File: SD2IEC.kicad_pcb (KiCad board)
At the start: 2 copper layers, 83.8 x 53.3 mm, 22 parts, among them J1 AVR-ISP-6, J2 Cassette Port, J3 SD_Card, J4 IEC Male, J5 IEC Female, U1 ATmega644P-20AU, U2 MIC5504-3.3YM5, Y1 8MHz

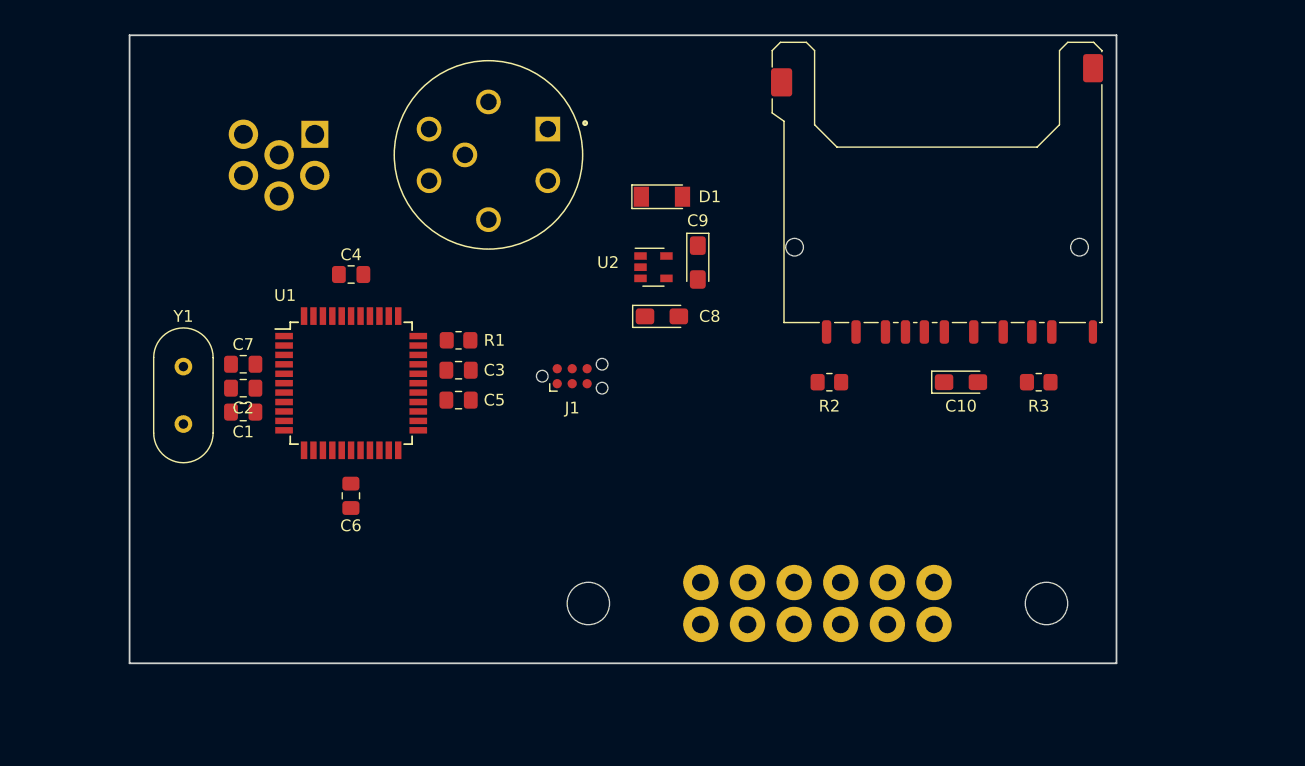
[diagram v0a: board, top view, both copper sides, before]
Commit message: Added IEC pin control
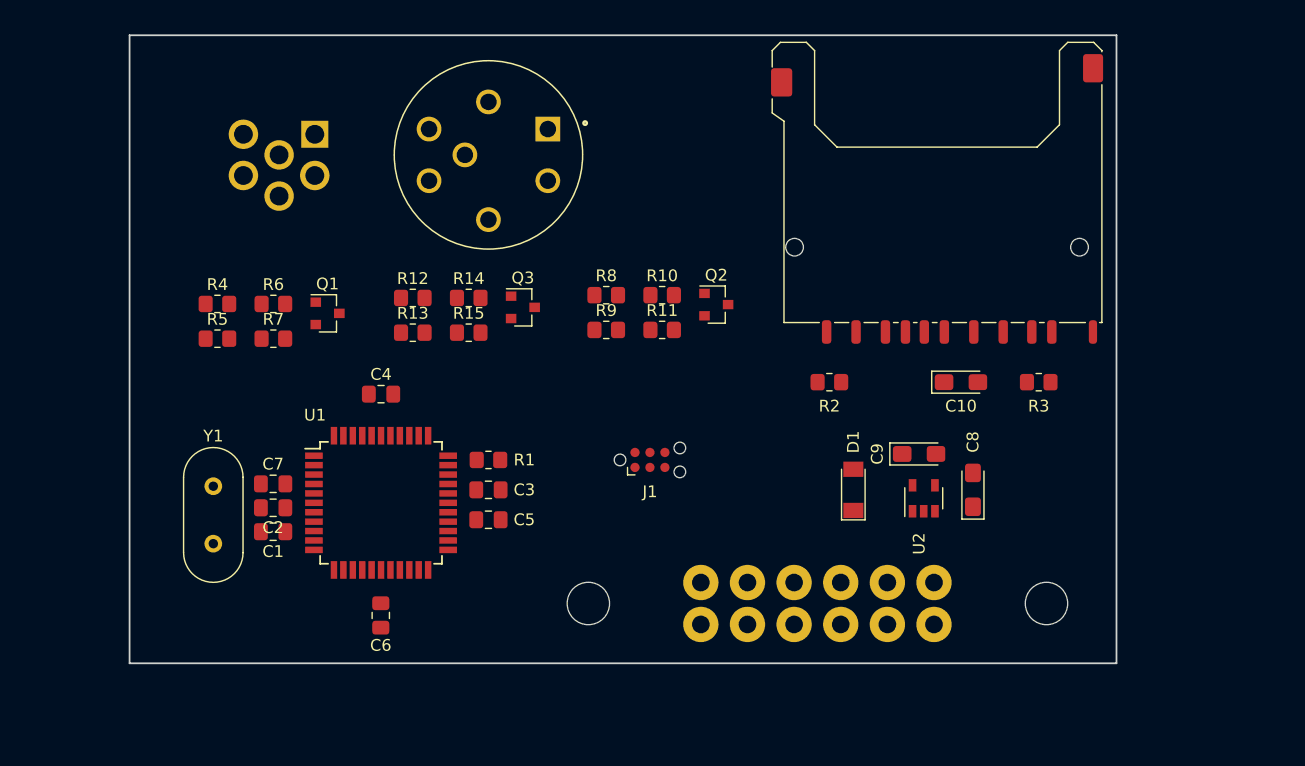
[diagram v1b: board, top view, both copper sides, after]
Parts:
- added Q1: BSS123, Package_TO_SOT_SMD:SOT-23, F.Cu at (100.6, 97.3)
- added Q2: BSS123, Package_TO_SOT_SMD:SOT-23, F.Cu at (133.7, 96.5)
- added Q3: BSS123, Package_TO_SOT_SMD:SOT-23, F.Cu at (117.2, 96.8)
- added R10: 10K, Resistor_SMD:R_0805_2012Metric_Pad1.20x1.40mm_HandSolder, F.Cu at (129.1, 95.7)
- added R11: 22K, Resistor_SMD:R_0805_2012Metric_Pad1.20x1.40mm_HandSolder, F.Cu at (129.1, 98.7)
- added R12: 10K, Resistor_SMD:R_0805_2012Metric_Pad1.20x1.40mm_HandSolder, F.Cu at (107.9, 96.0)
- added R13: 18R, Resistor_SMD:R_0805_2012Metric_Pad1.20x1.40mm_HandSolder, F.Cu at (107.9, 98.9)
- added R14: 10K, Resistor_SMD:R_0805_2012Metric_Pad1.20x1.40mm_HandSolder, F.Cu at (112.6, 96.0)
- added R15: 22K, Resistor_SMD:R_0805_2012Metric_Pad1.20x1.40mm_HandSolder, F.Cu at (112.6, 98.9)
- added R4: 10K, Resistor_SMD:R_0805_2012Metric_Pad1.20x1.40mm_HandSolder, F.Cu at (91.3, 96.5)
- added R5: 18R, Resistor_SMD:R_0805_2012Metric_Pad1.20x1.40mm_HandSolder, F.Cu at (91.3, 99.4)
- added R6: 10K, Resistor_SMD:R_0805_2012Metric_Pad1.20x1.40mm_HandSolder, F.Cu at (96.0, 96.5)
- added R7: 22K, Resistor_SMD:R_0805_2012Metric_Pad1.20x1.40mm_HandSolder, F.Cu at (96.0, 99.4)
- added R8: 10K, Resistor_SMD:R_0805_2012Metric_Pad1.20x1.40mm_HandSolder, F.Cu at (124.3, 95.7)
- added R9: 18R, Resistor_SMD:R_0805_2012Metric_Pad1.20x1.40mm_HandSolder, F.Cu at (124.3, 98.7)
- moved C8 30.2 mm to (155.4, 112.3), turned to 90 degrees
- moved U2 30.2 mm to (151.3, 113.0), turned to 90 degrees
- moved D1 29.7 mm to (145.3, 112.3), turned to 90 degrees
- moved C9 24.9 mm to (150.9, 109.2), turned to 0 degrees
- moved C6 10.5 mm to (105.2, 122.9)
- moved C7 10.5 mm to (96.0, 111.8)
- moved C5 10.5 mm to (114.3, 114.8)
- moved U1 10.5 mm to (105.2, 113.4)
- moved C1 10.5 mm to (96.0, 115.8)
- moved C2 10.5 mm to (96.0, 113.8)
- moved Y1 10.5 mm to (90.9, 116.8)
- moved C3 10.5 mm to (114.3, 112.3)
- moved C4 10.5 mm to (105.2, 104.1)
- moved R1 10.5 mm to (114.3, 109.7)
- moved J1 9.71 mm to (128.0, 109.7)
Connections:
- net IEC_ATN renamed /IEC_ATN
- net IEC_CLK renamed /IEC_CLK
- net IEC_DATA renamed /IEC_DATA
- net MISO renamed /MISO
- net MOSI renamed /MOSI
- net SCK renamed /SCK
- net ~IEC_RESET renamed /~IEC_RESET
- net ~IEC_SRQ renamed /~IEC_SQR
- net ~RESET renamed Net-(J1-Pad5)
- U1 pad 31: Net-(U1-Pad31) -> /IEC_CLK/WRITE
- U1 pad 32: Net-(U1-Pad32) -> /IEC_DATA/WRITE
- U1 pad 33: Net-(U1-Pad33) -> /IEC_ATN/WRITE
- U1 pad 35: Net-(U1-Pad35) -> /IEC_CLK/READ
- U1 pad 36: Net-(U1-Pad36) -> /IEC_DATA/READ
- U1 pad 37: Net-(U1-Pad37) -> /IEC_ATN/READ

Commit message: mosfets, switches
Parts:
- added J6: SERIAL, Connector_PinHeader_2.54mm:PinHeader_1x03_P2.54mm_Vertical, F.Cu at (91.4, 122.9)
- added SW1: IEC_SEL, Button_Switch_SMD:SW_DIP_SPSTx04_Slide_6.7x11.72mm_W8.61mm_P2.54mm_LowProfile, F.Cu at (127.0, 88.9)
- added SW2: Back, Button_Switch_THT:SW_Tactile_SPST_Angled_PTS645Vx58-2LFS, F.Cu at (118.9, 76.7)
- added SW3: Forward / Disc Change, Button_Switch_THT:SW_Tactile_SPST_Angled_PTS645Vx58-2LFS, F.Cu at (129.5, 76.7)
- Q1, Q2, Q3: value BSS123 -> AO3400A
- moved R10 21.4 mm to (107.7, 94.2)
- moved R11 21.4 mm to (107.7, 97.2)
- moved R8 21.4 mm to (103.0, 94.2)
- moved R9 21.4 mm to (103.0, 97.2)
- moved Q2 20.9 mm to (112.8, 95.5)
- moved Q3 17.4 mm to (134.1, 101.1)
- moved R12 16.6 mm to (124.1, 99.5)
- moved R13 16.6 mm to (124.1, 102.5)
- moved R14 16.6 mm to (128.9, 99.5)
- moved R15 16.6 mm to (128.9, 102.5)
- moved J5 7.13 mm to (107.2, 83.3)
- moved J4 5.18 mm to (91.4, 82.8)
- moved R5 4.37 mm to (87.7, 96.9)
- moved R7 4.37 mm to (92.5, 96.9)
- moved R4 4.37 mm to (87.7, 93.9)
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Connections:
- U1 pad 10: Net-(U1-Pad10) -> /TXD
- U1 pad 9: Net-(U1-Pad9) -> /RXD

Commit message: I2C Connector, cleanup
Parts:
- added J7: I2C, Connector_PinHeader_2.54mm:PinHeader_1x04_P2.54mm_Vertical, F.Cu at (108.2, 122.9)
- added SW4: RESET, Button_Switch_THT:SW_PUSH_6mm, F.Cu at (121.9, 108.7)
- SW1: footprint Button_Switch_SMD:SW_DIP_SPSTx04_Slide_6.7x11.72mm_W8.61mm_P2.54mm_LowProfile -> Button_Switch_THT:SW_DIP_SPSTx02_Slide_9.78x7.26mm_W7.62mm_P2.54mm
- SW2: value Back -> PREV
- SW3: value Forward / Disc Change -> NEXT
- moved J1 7.64 mm to (135.6, 110.2)
- moved SW1 4.57 mm to (131.6, 88.9), turned to 180 degrees
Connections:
- net /CARD_DETECT renamed /~CARD_DETECT
- net /WRITE_PROTECT renamed /~WRITE_PROTECT
- net Net-(SW1-Pad1) renamed /IEC10_11
- net Net-(SW1-Pad2) renamed /IEC8_9
- net Net-(SW2-Pad1) renamed /PREV
- net Net-(SW3-Pad1) renamed /NEXT
- SW1 pad 3: Net-(SW1-Pad3) -> GND
- SW1 pad 4: Net-(SW1-Pad4) -> GND
- U1 pad 23: Net-(U1-Pad23) -> /SCL
- U1 pad 24: Net-(U1-Pad24) -> /SDA
- U1 pad 25: Net-(U1-Pad25) -> /INTRQ

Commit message: Added status LEDs, Changed mcu to ATmega1284P (same footprint)
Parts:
- added D2: RED, LED_SMD:LED_0805_2012Metric_Pad1.15x1.40mm_HandSolder, F.Cu at (87.4, 101.1)
- added D3: GREEN, LED_SMD:LED_0805_2012Metric_Pad1.15x1.40mm_HandSolder, F.Cu at (87.4, 104.1)
- added R16: 330R, Resistor_SMD:R_0805_2012Metric_Pad1.20x1.40mm_HandSolder, F.Cu at (91.9, 104.1)
- added R17: 330R, Resistor_SMD:R_0805_2012Metric_Pad1.20x1.40mm_HandSolder, F.Cu at (92.1, 101.1)
- U1: value ATmega644P-20AU -> ATmega1284P-20AU
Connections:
- U1 pad 19: Net-(U1-Pad19) -> /BUSY_LED
- U1 pad 20: Net-(U1-Pad20) -> /DIRTY_LED

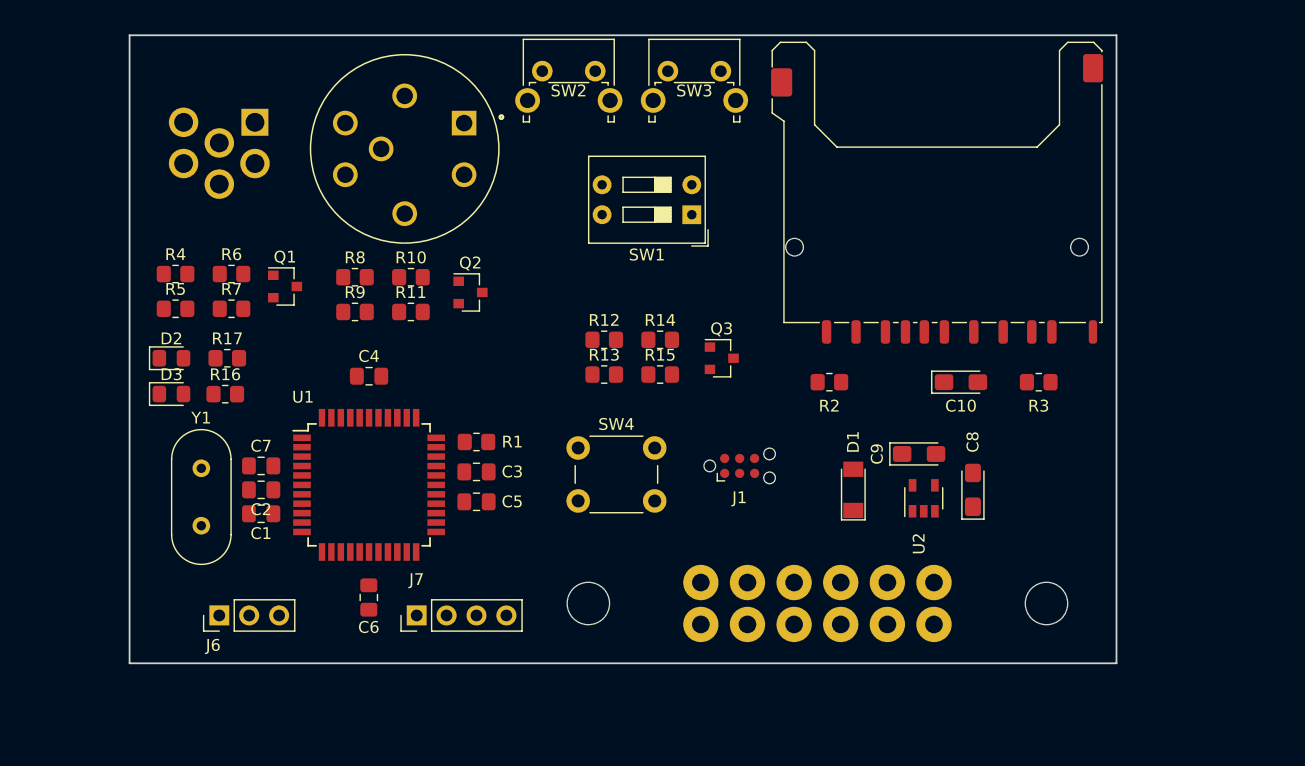
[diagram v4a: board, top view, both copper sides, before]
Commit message: Move cassette connector offboard
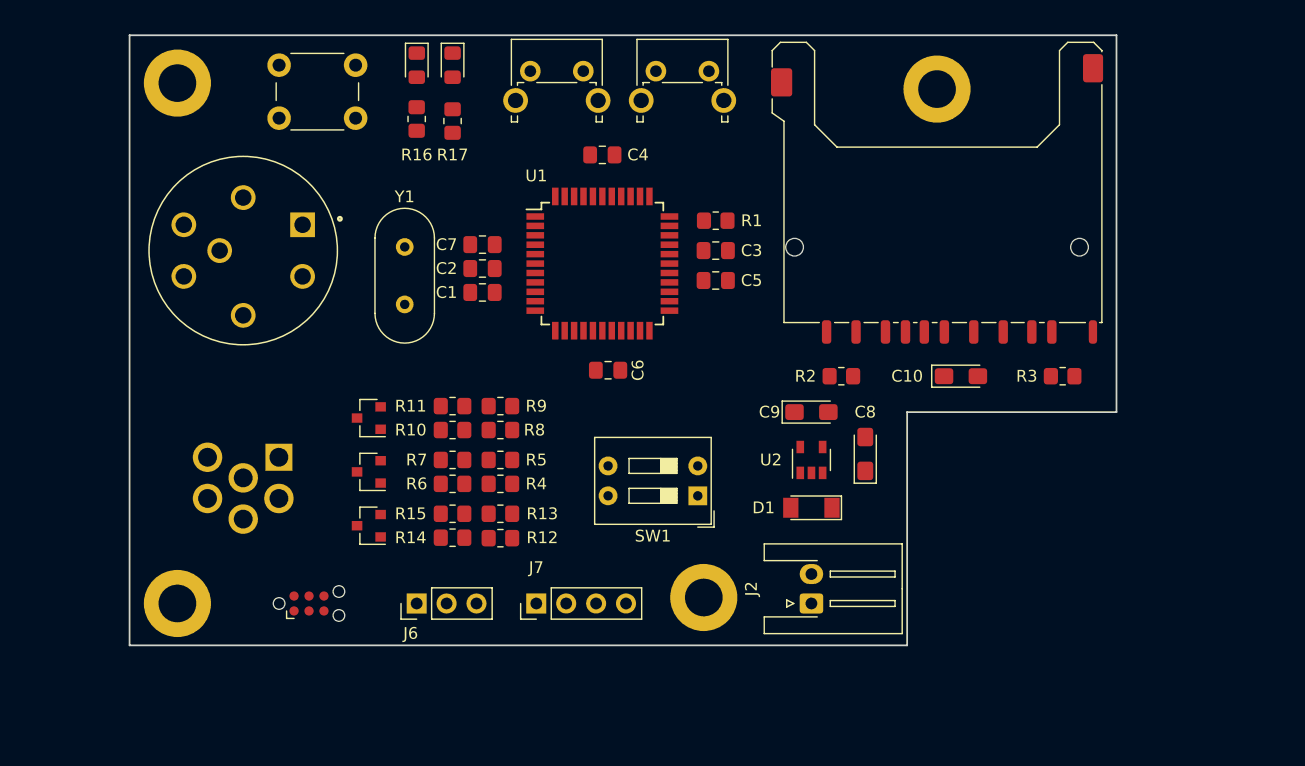
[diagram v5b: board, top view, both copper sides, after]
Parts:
- added H1: MountingHole_Pad, MountingHole:MountingHole_3.2mm_M3_ISO7380_Pad, F.Cu at (87.9, 77.7)
- added H2: MountingHole_Pad, MountingHole:MountingHole_3.2mm_M3_ISO7380_Pad, F.Cu at (152.4, 78.2)
- added H3: MountingHole_Pad, MountingHole:MountingHole_3.2mm_M3_ISO7380_Pad, F.Cu at (132.6, 121.4)
- added H4: MountingHole_Pad, MountingHole:MountingHole_3.2mm_M3_ISO7380_Pad, F.Cu at (87.9, 121.9)
- J2: value Cassette Port -> 5VDC IN; footprint DTLib:COMMODORE_CASSETTE -> Connector_JST:JST_XH_S2B-XH-A-1_1x02_P2.50mm_Horizontal; moved to F.Cu
- moved SW4 41.3 mm to (96.5, 76.2)
- moved J1 38.4 mm to (99.1, 121.9)
- moved D3 34.8 mm to (108.2, 76.2), turned to 270 degrees
- moved D2 34.5 mm to (111.3, 76.2), turned to 270 degrees
- moved Q3 33.2 mm to (104.1, 115.3), turned to 180 degrees
- moved R4 32.8 mm to (115.3, 111.8), turned to 180 degrees
- moved R5 30.4 mm to (115.3, 109.7), turned to 180 degrees
- moved J4 28.5 mm to (93.5, 111.3)
- moved R16 28.5 mm to (108.2, 80.8), turned to 270 degrees
- moved C6 28.0 mm to (124.5, 102.1), turned to 180 degrees
- moved R17 27.8 mm to (111.3, 80.9), turned to 270 degrees
- moved C3 27.7 mm to (133.6, 91.9)
- moved C5 27.7 mm to (133.6, 94.5)
- moved R1 27.7 mm to (133.6, 89.4)
- moved C4 27.3 mm to (124.0, 83.8)
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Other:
- board size 83.8 x 53.3 mm -> 83.8 x 51.8 mm

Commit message: Board orientation, DIN Connector
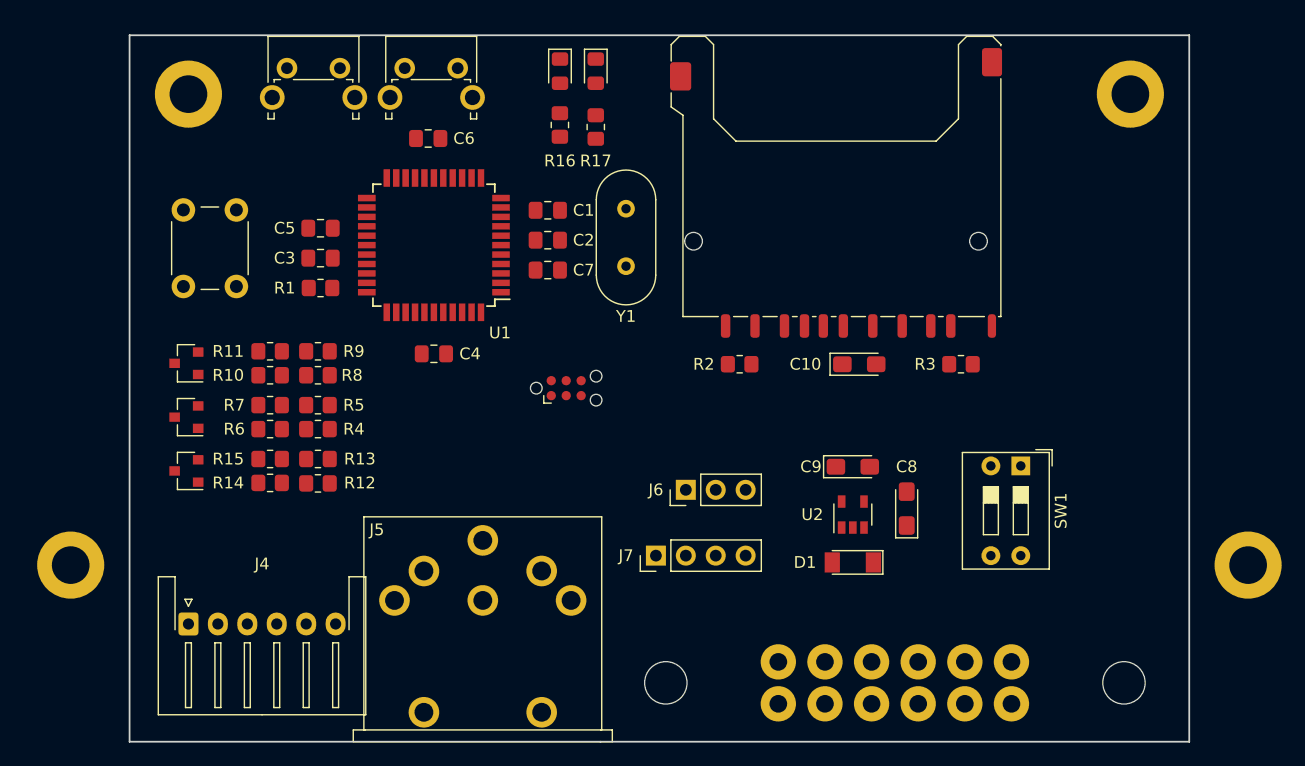
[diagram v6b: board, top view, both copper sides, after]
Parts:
- J2: footprint Connector_JST:JST_XH_S2B-XH-A-1_1x02_P2.50mm_Horizontal -> DTLib:COMMODORE_CASSETTE; moved to B.Cu
- J4: footprint DTLib:DIN6_MALE -> Connector_JST:JST_XH_S6B-XH-A-1_1x06_P2.50mm_Horizontal; moved to F.Cu
- J5: footprint DTLib:CUI_SD-60BV -> DTLib:DIN6_PCB_RIGHTANGLE
- moved H4 91.0 mm to (178.8, 118.7)
- moved H3 53.8 mm to (78.8, 118.7)
- moved J5 46.4 mm to (113.8, 133.7), turned to 0 degrees
- moved R1 34.1 mm to (100.0, 95.1), turned to 180 degrees
- moved C5 33.9 mm to (100.0, 90.0), turned to 0 degrees
- moved C3 33.6 mm to (100.0, 92.6), turned to 0 degrees
- moved J1 28.5 mm to (120.9, 103.6)
- moved SW1 27.5 mm to (159.5, 110.2), turned to 270 degrees
- moved C6 24.9 mm to (109.2, 82.4), turned to 0 degrees
- moved J6 24.8 mm to (131.1, 112.3)
- moved C4 22.1 mm to (109.7, 100.7), turned to 180 degrees
- moved SW3 21.3 mm to (107.2, 76.5)
- moved SW2 20.7 mm to (97.2, 76.5)
- moved SW4 20.5 mm to (88.4, 95.0), turned to 90 degrees
- moved Y1 20.5 mm to (126.0, 88.4), turned to 270 degrees
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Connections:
- J2 pad 1: +5V -> GND
- J2 pad 2: GND -> +5V
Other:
- board size 83.8 x 51.8 mm -> 90 x 60 mm

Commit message: Switched to horizontal compact layout
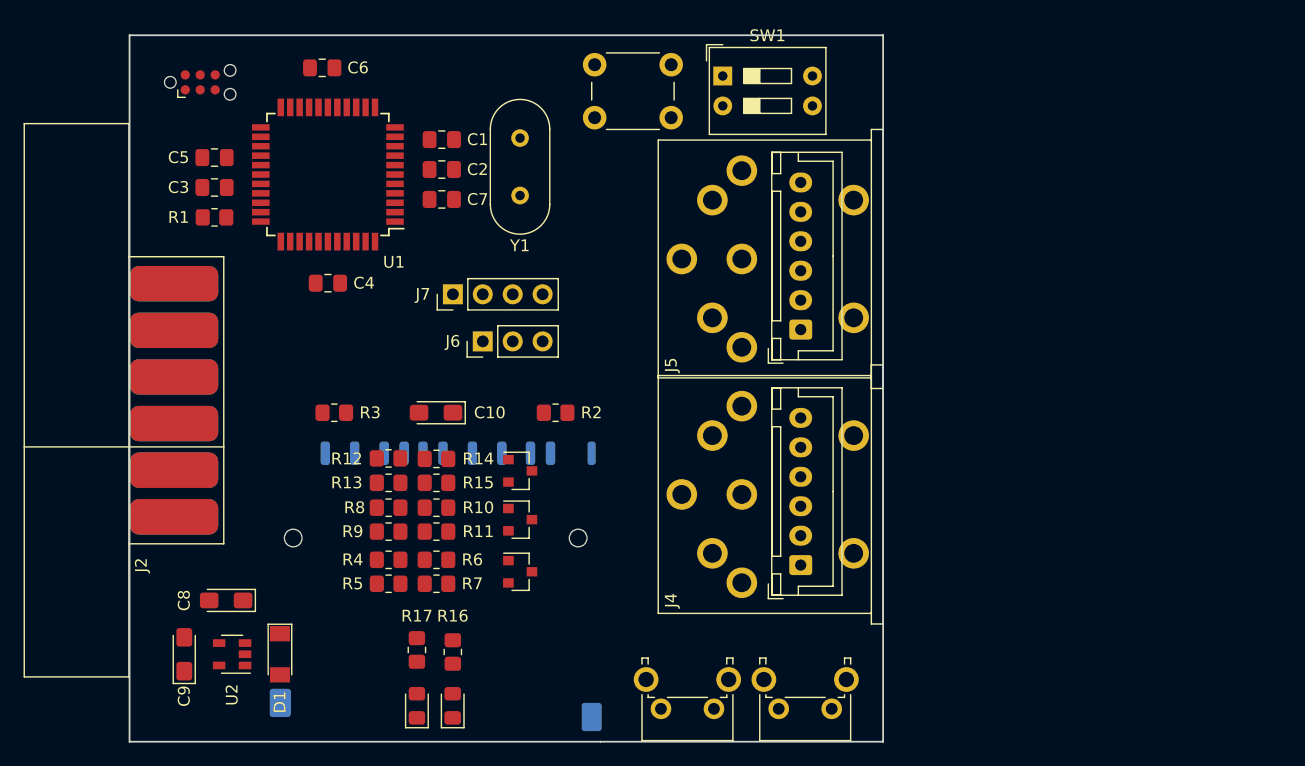
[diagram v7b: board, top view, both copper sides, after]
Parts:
- removed H1, H2, H3, H4: MountingHole_Pad, MountingHole:MountingHole_3.2mm_M3_ISO7380_Pad
- added J8: IEC_ALT1, Connector_JST:JST_XH_B6B-XH-A_1x06_P2.50mm_Vertical, F.Cu at (140.8, 118.7)
- added J9: IEC_ALT2, Connector_JST:JST_XH_B6B-XH-A_1x06_P2.50mm_Vertical, F.Cu at (140.8, 98.7)
- J2: footprint DTLib:COMMODORE_CASSETTE -> DTLib:COMMODORE_CASSETTE_EdgeMount; moved to F.Cu
- J3: moved to B.Cu
- J4: value IEC Male -> IEC (DIN6); footprint Connector_JST:JST_XH_S6B-XH-A-1_1x06_P2.50mm_Horizontal -> DTLib:DIN6_PCB_RIGHTANGLE
- J5: value IEC Female -> IEC (DIN6)
- moved SW2 71.4 mm to (143.5, 130.9), turned to 180 degrees
- moved J2 69.3 mm to (83.8, 104.7), turned to 270 degrees
- moved SW3 60.4 mm to (133.5, 130.9), turned to 180 degrees
- moved J4 60.0 mm to (147.8, 112.7), turned to 90 degrees
- moved C9 59.0 mm to (88.5, 126.2), turned to 90 degrees
- moved C8 58.3 mm to (92.0, 121.7), turned to 180 degrees
- moved D2 56.0 mm to (108.2, 130.6), turned to 90 degrees
- moved D3 54.7 mm to (111.3, 130.6), turned to 90 degrees
- moved U2 54.0 mm to (92.5, 126.2), turned to 180 degrees
- moved R3 53.4 mm to (101.2, 105.7), turned to 0 degrees
- moved J5 53.3 mm to (147.8, 92.7), turned to 90 degrees
- moved J3 49.4 mm to (109.8, 121.7)
- moved D1 49.3 mm to (96.6, 126.2), turned to 270 degrees
- moved R17 46.9 mm to (108.2, 125.9), turned to 90 degrees
- moved R16 45.7 mm to (111.3, 126.0), turned to 90 degrees
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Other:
- board size 90 x 60 mm -> 64 x 60 mm
